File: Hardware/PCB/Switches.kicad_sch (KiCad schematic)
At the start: 73 parts, among them U10 SW_MX_HE, U11 SW_MX_HE, U12 SW_MX_HE, U13 SW_MX_HE, U14 SW_MX_HE, U15 SW_MX_HE, U16 SW_MX_HE, U17 SW_MX_HE, U18 SW_MX_HE, U19 SW_MX_HE, U20 SW_MX_HE, U21 SW_MX_HE, U22 SW_MX_HE, U23 SW_MX_HE, U24 SW_MX_HE, U25 SW_MX_HE, U26 SW_MX_HE, U27 SW_MX_HE, U28 SW_MX_HE, U29 SW_MX_HE, U30 SW_MX_HE, U31 SW_MX_HE, U32 SW_MX_HE, U33 SW_MX_HE, U34 SW_MX_HE, U35 SW_MX_HE, U36 SW_MX_HE, U37 SW_MX_HE, U38 SW_MX_HE, U39 SW_MX_HE, U40 SW_MX_HE, U41 SW_MX_HE, U42 SW_MX_HE, U43 SW_MX_HE, U44 SW_MX_HE, U45 SW_MX_HE, U46 SW_MX_HE, U47 SW_MX_HE, U48 SW_MX_HE, U49 SW_MX_HE, U5 CD74HC4067M, U50 SW_MX_HE, U51 SW_MX_HE, U52 SW_MX_HE, U53 SW_MX_HE, U54 SW_MX_HE, U55 SW_MX_HE, U56 SW_MX_HE, U57 SW_MX_HE, U58 SW_MX_HE, U59 SW_MX_HE, U6 CD74HC4067M, U60 SW_MX_HE, U61 SW_MX_HE, U62 SW_MX_HE, U63 SW_MX_HE, U64 SW_MX_HE, U65 SW_MX_HE, U66 SW_MX_HE, U67 SW_MX_HE, U68 SW_MX_HE, U69 SW_MX_HE, U7 CD74HC4067M, U70 SW_MX_HE, U71 SW_MX_HE, U72 SW_MX_HE, U73 SW_MX_HE, U74 SW_MX_HE, U75 SW_MX_HE, U76 SW_MX_HE, U77 SW_MX_HE, U8 CD74HC4067M, U9 CD74HC4067M

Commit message: Connected everything with the new rp2350 setup
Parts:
- removed U77: SW_MX_HE, PCM_marbastlib-he:SW_MX_HE_0deg_1u, symbol PCM_marbastlib-he:SW_MX_HE
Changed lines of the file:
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@@
 	(wire
 		(pts
-			(xy 472.44 193.04) (xy 491.49 193.04)
-		)
-		(stroke
-			(width 0)
-			(type default)
-		)
-	)
-	(wire
-		(pts
 			(xy 410.21 119.38) (xy 410.21 193.04)
 		)
@@
 	(wire
 		(pts
-			(xy 464.82 88.9) (xy 472.44 88.9)
-		)
-		(stroke
-			(width 0)
-			(type default)
-		)
-	)
-	(wire
-		(pts
 			(xy 228.6 194.31) (xy 247.65 194.31)
 		)
@@
 	(wire
 		(pts
-			(xy 472.44 88.9) (xy 472.44 193.04)
-		)
-		(stroke
-			(width 0)
-			(type default)
-		)
-	)
-	(wire
-		(pts
 			(xy 340.36 93.98) (xy 382.27 93.98)
 		)
@@
 	)
 	(symbol
-		(lib_id "power:GND")
-		(at 481.33 203.2 0)
-		(unit 1)
-		(body_style 1)
-		(exclude_from_sim no)
-		(in_bom yes)
-		(on_board yes)
-		(in_pos_files yes)
-		(dnp no)
-		(fields_autoplaced yes)
-		(property "Reference" "#PWR0161"
-			(at 481.33 209.55 0)
-			(hide yes)
-			(show_name no)
-			(do_not_autoplace no)
-			(effects
-				(font
-					(size 1.27 1.27)
-				)
-			)
-		)
-		(property "Value" "GND"
-			(at 481.33 208.28 0)
-			(show_name no)
-			(do_not_autoplace no)
-			(effects
-				(font
-					(size 1.27 1.27)
-				)
-			)
-		)
-		(property "Footprint" ""
-			(at 481.33 203.2 0)
-			(hide yes)
-			(show_name no)
-			(do_not_autoplace no)
-			(effects
-				(font
-					(size 1.27 1.27)
-				)
-			)
-		)
-		(property "Datasheet" ""
-			(at 481.33 203.2 0)
-			(hide yes)
-			(show_name no)
-			(do_not_autoplace no)
-			(effects
-				(font
-					(size 1.27 1.27)
-				)
-			)
-		)
-		(property "Description" "Power symbol creates a global label with name \"GND\" , ground"
-			(at 481.33 203.2 0)
-			(hide yes)
-			(show_name no)
-			(do_not_autoplace no)
-			(effects
-				(font
-					(size 1.27 1.27)
-				)
-			)
-		)
-		(pin "1"
-		)
-		(instances
-			(project "VNTR-65"
-				(path "/9381cecd-296d-4002-be35-b038a1e96b55/035a10d1-8b88-4317-ad70-2839e681f0d1"
-					(reference "#PWR0161")
-					(unit 1)
-				)
-			)
-		)
-	)
-	(symbol
 		(lib_id "PCM_marbastlib-he:SW_MX_HE")
 		(at 297.18 97.79 0)
@@
 	(symbol
 		(lib_id "PCM_marbastlib-he:SW_MX_HE")
-		(at 483.87 193.04 0)
-		(unit 1)
-		(body_style 1)
-		(exclude_from_sim no)
-		(in_bom yes)
-		(on_board yes)
-		(in_pos_files yes)
-		(dnp no)
-		(fields_autoplaced yes)
-		(property "Reference" "U77"
-			(at 477.52 191.7699 0)
-			(show_name no)
-			(do_not_autoplace no)
-			(effects
-				(font
-					(size 1.27 1.27)
-				)
-				(justify right)
-			)
-		)
-		(property "Value" "SW_MX_HE"
-			(at 477.52 194.3099 0)
-			(show_name no)
-			(do_not_autoplace no)
-			(effects
-				(font
-					(size 1.27 1.27)
-				)
-				(justify right)
-			)
-		)
-		(property "Footprint" "PCM_marbastlib-he:SW_MX_HE_0deg_1u"
-			(at 483.87 201.93 0)
-			(hide yes)
-			(show_name no)
-			(do_not_autoplace no)
-			(effects
-				(font
-					(size 1.27 1.27)
-					(italic yes)
-				)
-				(justify left)
-			)
-		)
-		(property "Datasheet" "https://wmsc.lcsc.com/wmsc/upload/file/pdf/v2/lcsc/2310271810_Hallwee-HAL9303SO_C19089525.pdf"
-			(at 483.87 176.53 0)
-			(hide yes)
-			(show_name no)
-			(do_not_autoplace no)
-			(effects
-				(font
-					(size 1.27 1.27)
-				)
-			)
-		)
-		(property "Description" "Hall effect switch, bipolar, -+1000Gs, 4.7mV/Gs, -40C to +150C, SOT-23"
-			(at 483.87 193.04 0)
-			(hide yes)
-			(show_name no)
-			(do_not_autoplace no)
-			(effects
-				(font
-					(size 1.27 1.27)
-				)
-			)
-		)
-		(pin "3"
-		)
-		(pin "1"
-		)
-		(pin "2"
-		)
-		(instances
-			(project "VNTR-65"
-				(path "/9381cecd-296d-4002-be35-b038a1e96b55/035a10d1-8b88-4317-ad70-2839e681f0d1"
-					(reference "U77")
-					(unit 1)
-				)
-			)
-		)
-	)
-	(symbol
-		(lib_id "PCM_marbastlib-he:SW_MX_HE")
 		(at 121.92 195.58 0)
 		(unit 1)
@@
 		(members "11fb9480-f201-475a-8a1f-afae020eb6f0" "133ffc07-4d01-411c-96d6-13f9bd20c375"
 			"1347f9d9-9eff-4800-aa6d-fd5be2b8fefe" "143594d9-ca0a-4e0c-88be-19ea848d02c5"
-			"1ebc6f74-e69c-4f99-808e-e0dd2b7f3d0e" "2a5b67cb-3aed-4c61-baeb-8eb9f4ebfc48"
-			"325dfff5-840d-4bd2-8f76-67361cdb2db4" "359fcdbe-596c-4342-a48d-dde6cdf9adec"
+			"2a5b67cb-3aed-4c61-baeb-8eb9f4ebfc48" "325dfff5-840d-4bd2-8f76-67361cdb2db4"
 			"36445c2d-9237-456e-b308-9f4f945e722e" "39ed282c-60a9-4248-aaa9-0dfa82ff2fd0"
 			"541c0de8-66e5-4a23-8167-1cfc4092fd40" "68ad9e26-f62c-4df9-ae84-3036ebde04da"
 			"69f7c49c-0018-4596-aae1-01284979eb1b" "8b6fbdbc-3ad3-408f-882c-7ff58a87f97f"
 			"a7a50ae4-ba6f-4979-92f0-af2a72fb4214" "ab4302f8-60e2-4168-86c3-e64659942d2b"
-			"ada1f900-17c3-4811-8cd3-902aa9cb8280" "b273bb1b-6437-44bd-90cd-ebf55d5907e1"
 			"be60cc36-e398-4ab5-8d0c-01106e09cae7" "c7e76322-bb28-454f-9b31-5e72b624f369"
-			"d0428ff2-9ced-4dec-9770-675918a293d8" "e22e538d-28a7-4b5e-824b-cbc698852630"
-			"e3d279df-3ca6-4ebb-b02b-c96e8f9aec55" "e4c3276a-bf3a-4c78-a8e2-8d1a1827fddb"
-			"f3ef8a17-88fa-4963-bb24-0f07b0ee77eb" "fffffc29-9180-413d-a75b-d0feebca5d09"
+			"d0428ff2-9ced-4dec-9770-675918a293d8" "e3d279df-3ca6-4ebb-b02b-c96e8f9aec55"
+			"e4c3276a-bf3a-4c78-a8e2-8d1a1827fddb" "f3ef8a17-88fa-4963-bb24-0f07b0ee77eb"
+			"fffffc29-9180-413d-a75b-d0feebca5d09"
 		)
 	)

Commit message: Refined the pcb design overall
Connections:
- net +3.3V renamed +3V3

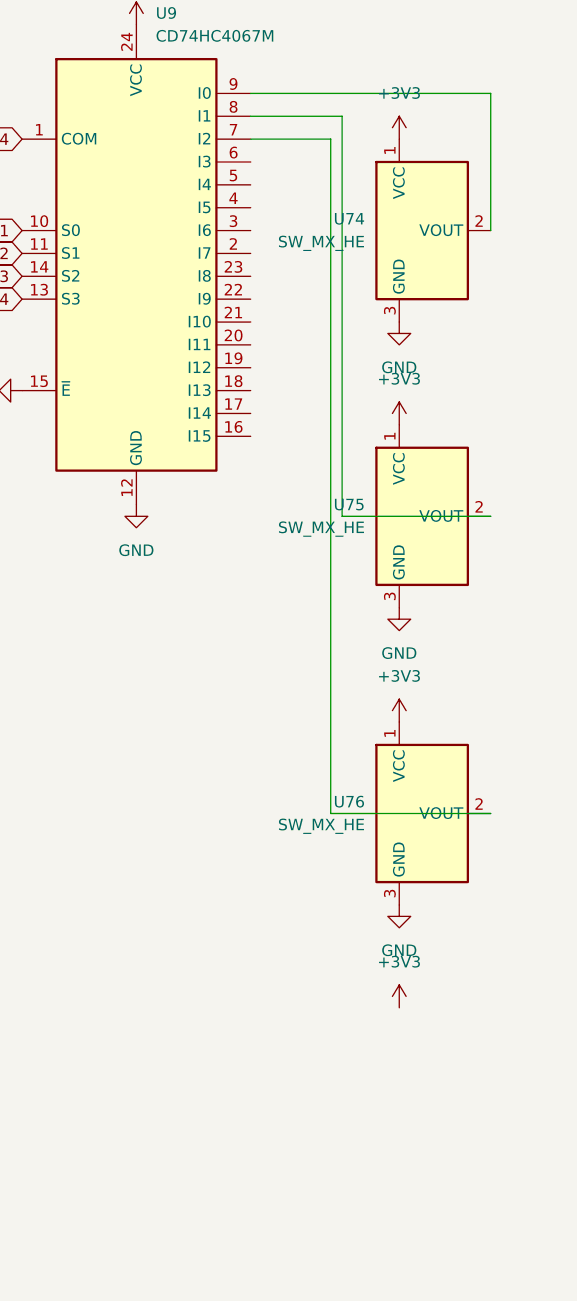
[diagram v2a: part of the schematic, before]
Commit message: Update pcb to smaller size
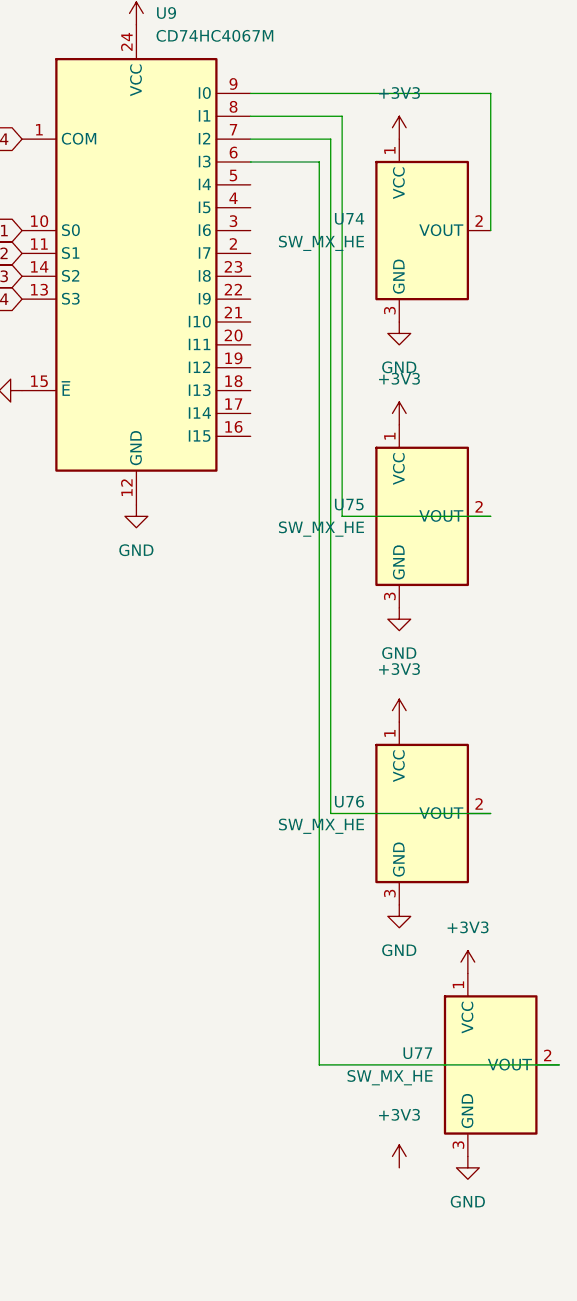
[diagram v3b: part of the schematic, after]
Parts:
- added U77: SW_MX_HE, PCM_marbastlib-he:SW_MX_HE_0deg_1u, symbol PCM_marbastlib-he:SW_MX_HE
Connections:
- net +3V3: now also U77.1 (VCC)
- net GND: now also U77.3 (GND)
- net at U9.6 (I3): now also U77.2 (VOUT)
